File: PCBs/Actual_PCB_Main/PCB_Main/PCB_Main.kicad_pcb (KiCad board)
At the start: 2 copper layers, 145 parts, among them J1 fan connector, J10 To_Speaker_R, J2 10118193-0001LF, J4 10118193-0001LF, J6 XT60-M, J7 HUB75, J9 To_Speaker_L, M1 CSD17581Q3, M2 CSD17581Q3A, Q1 S8050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

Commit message: started PCB Layout
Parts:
- J1: value fan connector -> fanpin
- J2: value 10118193-0001LF -> WBoot
- J4: value 10118193-0001LF -> RBoot
- Q4: value Fan_NMOS -> FanMOS
- R20: footprint Resistor_SMD:R_0815_2038Metric -> Resistor_SMD:R_0805_2012Metric
- U1: value CP2102N-Axx-xQFN28 -> WBootChip
- U9: value CP2102N-Axx-xQFN28 -> RBootChip
- Y2: value CB3LV-3I-40M000000 -> RCLK
- moved J2 178.8 mm to (128.1, 14.3), turned to 180 degrees
- moved C3 162.4 mm to (121.3, 20.6), turned to 90 degrees
- moved Cin1 160.6 mm to (294.4, 172.9)
- moved Cout1 160.6 mm to (280.3, 165.3)
- moved Coutx1 160.6 mm to (293.6, 193.0)
- moved Cres1 160.6 mm to (262.6, 205.7)
- moved Css1 160.6 mm to (277.8, 195.6)
- moved Cvcc1 160.6 mm to (276.9, 202.7)
- moved Dbst1 160.6 mm to (254.0, 205.7)
- moved H1 160.6 mm to (351.5, 285.7)
- moved H2 160.6 mm to (351.5, 278.7)
- moved L1 160.6 mm to (243.8, 172.7)
- moved Rfbt1 160.6 mm to (283.6, 202.4)
- moved Rslope1 160.6 mm to (286.1, 195.6)
- moved Rt1 160.6 mm to (293.0, 182.9)
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- renumbered LightSensorConnector1 to +LightGND, Boot2WROOM1 to WBoot2
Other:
- board text added: "GND"
- board text added: "VDD"

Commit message: PCB reset traces
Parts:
- added Cout1: 560.0 uF, Artisyn_Components:PCAP_SVP_F12_PAN, F.Cu at (257.8, -6.60)
- added Cout1: 560.0 uF, Artisyn_Components:PCAP_SVP_F12_PAN, F.Cu at (257.8, -20.8)
- moved Cvcc1 202.0 mm to (379.4, 28.8)
- moved Rfbt1 202.0 mm to (386.1, 28.4)
- moved Rt1 202.0 mm to (395.6, 8.89)
- moved Coutx1 202.0 mm to (396.1, 19.1)
- moved Cvin1 202.0 mm to (372.7, 29.2)
- moved Cbst1 202.0 mm to (366.7, 22.7)
- moved Rvin1 195.3 mm to (326.5, 11.9)
- moved Cin1 189.9 mm to (223.6, -3.30)
- moved Rfbb1 179.3 mm to (392.2, 46.5)
- moved Rsense1 166.3 mm to (226.3, 33.5), turned to 90 degrees
- moved Cout1 159.0 mm to (257.9, 7.87)
- moved R21 155.9 mm to (89.0, 43.4)
- moved R19 153.5 mm to (89.0, 47.0)
- moved M1 148.3 mm to (252.5, 28.9), turned to -90 degrees
- moved M2 141.4 mm to (263.0, 41.9)
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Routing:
- net TXD0_ROVER: track 0.00 -> 89.0 mm, vias 0 -> 6
- net EN_ROVER: track 0.00 -> 86.0 mm, vias 0 -> 2
- net RXD0_ROVER: track 0.00 -> 65.7 mm, vias 0 -> 4
- net RXD0_WROOM: track 0.00 -> 51.2 mm, vias 0 -> 2
- net TXD0_WROOM: track 0.00 -> 49.1 mm, vias 0 -> 4
- net 3.3V: track 0.00 -> 43.7 mm
- net GND: track 0.00 -> 42.2 mm
- net DTR_WROOM: track 0.00 -> 35.0 mm
- net DTR_ROVER: track 0.00 -> 32.7 mm, vias 0 -> 3
- net RTS_WROOM: track 0.00 -> 27.6 mm, vias 0 -> 3
- net IO0_ROVER: track 0.00 -> 26.3 mm
- net USB_DN_WROOM: track 0.00 -> 20.3 mm, vias 0 -> 2
- net EN_WROOM: track 0.00 -> 19.4 mm
- net USB_DP_ROVER: track 0.00 -> 18.9 mm, vias 0 -> 2
- net VBUS_ROVER: track 0.00 -> 17.5 mm, vias 0 -> 2
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
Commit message: Add files via upload
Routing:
- net 3.3V: track 43.7 -> 64.6 mm
- net GND: track 42.2 -> 61.0 mm
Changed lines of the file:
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@@
   (segment (start 70.104 56.134) (end 72.2395 56.134) (width 0.25) (layer "F.Cu") (net 3))
   (segment (start 67.065 55.38) (end 69.35 55.38) (width 0.25) (layer "F.Cu") (net 3))
+  (segment (start 48.937499 22.712499) (end 53.104999 22.712499) (width 0.25) (layer "F.Cu") (net 4))
   (segment (start 60.96 48.768) (end 60.96 48.26) (width 0.25) (layer "F.Cu") (net 4))
   (segment (start 98.334999 16.839999) (end 95.794999 14.299999) (width 0.25) (layer "F.Cu") (net 4))
+  (segment (start 120.5465 29.464) (end 121.056 29.464) (width 0.25) (layer "F.Cu") (net 4))
   (segment (start 45.72 68.58) (end 47.31 70.17) (width 0.25) (layer "F.Cu") (net 4))
   (segment (start 116.84 20.508) (end 118.11 20.508) (width 0.25) (layer "F.Cu") (net 4))
@@
   (segment (start 105.28 70.358) (end 105.28 69.4925) (width 0.25) (layer "F.Cu") (net 4))
   (segment (start 118.11 20.508) (end 118.684 21.082) (width 0.25) (layer "F.Cu") (net 4))
+  (segment (start 49.408 26.924) (end 49.408 28.954) (width 0.25) (layer "F.Cu") (net 4))
   (segment (start 58.184999 17.639999) (end 59.104999 16.719999) (width 0.25) (layer "F.Cu") (net 4))
+  (segment (start 53.104999 23.227001) (end 49.408 26.924) (width 0.25) (layer "F.Cu") (net 4))
   (segment (start 47.31 70.17) (end 48.26 70.17) (width 0.25) (layer "F.Cu") (net 4))
+  (segment (start 121.056 29.464) (end 125.12 33.528) (width 0.25) (layer "F.Cu") (net 4))
+  (segment (start 53.104999 22.712499) (end 53.104999 23.227001) (width 0.25) (layer "F.Cu") (net 4))
   (segment (start 61.087 49.657) (end 60.96 49.53) (width 0.25) (layer "F.Cu") (net 4))
   (segment (start 62 52.315) (end 62 50.57) (width 0.25) (layer "F.Cu") (net 4))
+  (segment (start 48.024999 21.799999) (end 48.937499 22.712499) (width 0.25) (layer "F.Cu") (net 4))
   (segment (start 62.5 52.315) (end 62.5 50.308) (width 0.25) (layer "F.Cu") (net 4))
   (segment (start 102.74 72.71) (end 102.74 70.996) (width 0.25) (layer "F.Cu") (net 4))
@@
   (segment (start 49.022 60.96) (end 48.768 60.706) (width 0.25) (layer "F.Cu") (net 4))
   (segment (start 58.154999 17.669999) (end 58.184999 17.639999) (width 0.25) (layer "F.Cu") (net 4))
+  (segment (start 49.408 28.954) (end 50.358 29.904) (width 0.25) (layer "F.Cu") (net 4))
   (segment (start 59.104999 16.719999) (end 61.004999 16.719999) (width 0.25) (layer "F.Cu") (net 4))
   (segment (start 113.574999 21.839999) (end 115.508001 21.839999) (width 0.25) (layer "F.Cu") (net 4))
@@
   (segment (start 102.74 74.61) (end 103.69 74.61) (width 0.25) (layer "F.Cu") (net 6))
   (segment (start 241.874 151.226) (end 241.874 150.18) (width 0.25) (layer "F.Cu") (net 6))
+  (segment (start 51.308 26.924) (end 54.488 26.924) (width 0.25) (layer "F.Cu") (net 6))
   (segment (start 64.45 45.654) (end 64.262 45.466) (width 0.25) (layer "F.Cu") (net 6))
   (segment (start 75.33 68.58) (end 72.79 68.58) (width 0.25) (layer "F.Cu") (net 6))
@@
   (segment (start 64.45 48.26) (end 64.45 45.654) (width 0.25) (layer "F.Cu") (net 6))
   (segment (start 242.316 151.668) (end 241.874 151.226) (width 0.25) (layer "F.Cu") (net 6))
+  (segment (start 54.488 23.906998) (end 54.488 26.924) (width 0.25) (layer "F.Cu") (net 6))
+  (segment (start 55.644999 22.749999) (end 54.488 23.906998) (width 0.25) (layer "F.Cu") (net 6))
   (segment (start 45.72 73.66) (end 47.31 72.07) (width 0.25) (layer "F.Cu") (net 6))
   (segment (start 64.516 49.53) (end 64.516 48.768) (width 0.25) (layer "F.Cu") (net 6))
@@
   (segment (start 47.31 72.07) (end 48.26 72.07) (width 0.25) (layer "F.Cu") (net 6))
   (segment (start 58.474999 15.449999) (end 58.184999 15.739999) (width 0.25) (layer "F.Cu") (net 6))
+  (segment (start 132.78 24.209998) (end 134.369999 22.619999) (width 0.25) (layer "F.Cu") (net 6))
   (segment (start 58.154999 15.769999) (end 58.184999 15.739999) (width 0.25) (layer "F.Cu") (net 6))
   (segment (start 63.942 47.752) (end 64.45 48.26) (width 0.25) (layer "F.Cu") (net 6))
@@
   (segment (start 77.43 75.76) (end 77.43 75.732) (width 0.25) (layer "F.Cu") (net 6))
   (segment (start 100.234999 14.939999) (end 100.874999 14.299999) (width 0.25) (layer "F.Cu") (net 6))
+  (segment (start 55.644999 15.769999) (end 48.974999 15.769999) (width 0.25) (layer "F.Cu") (net 6))
   (segment (start 64 50.554) (end 64.008 50.546) (width 0.25) (layer "F.Cu") (net 6))
   (segment (start 100.234999 16.839999) (end 100.234999 14.939999) (width 0.25) (layer "F.Cu") (net 6))
@@
   (segment (start 106.68 73.02) (end 109.22 70.48) (width 0.25) (layer "F.Cu") (net 6))
   (segment (start 55.644999 15.769999) (end 58.154999 15.769999) (width 0.25) (layer "F.Cu") (net 6))
+  (segment (start 132.78 24.892) (end 132.78 24.209998) (width 0.25) (layer "F.Cu") (net 6))
+  (segment (start 48.974999 15.769999) (end 48.024999 16.719999) (width 0.25) (layer "F.Cu") (net 6))
   (segment (start 110.009999 26.904999) (end 110.009999 31.214001) (width 0.25) (layer "F.Cu") (net 8))
   (segment (start 110.009999 31.214001) (end 109.22 32.004) (width 0.25) (layer "F.Cu") (net 8))

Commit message: pcb almost done
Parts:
- added C35: 1000uF, Artisyn_Components:Audio_1000uF, F.Cu at (141.7, 23.4)
- added D2: RED LED, LED_SMD:LED_0805_2012Metric, F.Cu at (136.4, 35.6)
- added R26: 1k, Resistor_SMD:R_0805_2012Metric, F.Cu at (140.2, 36.6)
- J1: value fanpin -> fan connector
- J2: value WBoot -> 10118193-0001LF
- J4: value RBoot -> 10118193-0001LF
- Q4: value FanMOS -> Fan_NMOS
- U1: value WBootChip -> CP2102N-Axx-xQFN28
- U9: value RBootChip -> CP2102N-Axx-xQFN28
- Y2: value RCLK -> CB3LV-3I-40M000000
- moved CsnL1 84.9 mm to (175.2, 105.5)
- moved RsnL1 84.9 mm to (175.2, 110.5)
- moved C0L1 84.0 mm to (189.5, 106.9)
- moved CsnR1 84.0 mm to (162.0, 100.1)
- moved J10 84.0 mm to (136.4, 109.2)
- moved C0R1 84.0 mm to (146.0, 108.7)
- moved CiL1 84.0 mm to (172.2, 100.5)
- moved CiR1 84.0 mm to (157.5, 110.2)
- moved Csc1 84.0 mm to (168.9, 110.3)
- moved J9 84.0 mm to (203.7, 106.4)
- moved RsnR1 84.0 mm to (162.0, 104.8)
- moved U7 84.0 mm to (168.4, 121.4)
- moved C3b1 84.0 mm to (191.2, 120.1)
- moved Cb1 84.0 mm to (161.0, 90.4)
- moved C21 32.6 mm to (137.2, 67.6), turned to 180 degrees
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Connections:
- Boot2ROVER1 pad 2: RXD0_ROVER -> Net-(Boot2ROVER1-RX)
- Boot2ROVER1 pad 3: TXD0_ROVER -> Net-(Boot2ROVER1-TX)
- Rsense1 pad 1: Net-(U5-CSN) -> 5V
- Rsense1 pad 2: 5V -> Net-(U5-CSN)
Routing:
- net WROOM_TO_FANS: track 0.00 -> 135.2 mm, vias 0 -> 4
- net GND: track 61.0 -> 195.1 mm, vias 0 -> 39
- net 5V: track 0.00 -> 99.8 mm
- net AGND: track 0.00 -> 75.2 mm, vias 0 -> 3
- net STB: track 0.00 -> 70.4 mm, vias 0 -> 2
- net C_PIN: track 0.00 -> 67.8 mm, vias 0 -> 3
- net I2S-WS: track 0.00 -> 65.6 mm, vias 0 -> 2
- net A_PIN: track 0.00 -> 61.5 mm, vias 0 -> 2
- net CLK_PIN: track 0.00 -> 59.3 mm, vias 0 -> 2
- net WROOM_TALK_TX: track 0.00 -> 58.6 mm, vias 0 -> 5
- net WROOM_TALK_RX: track 0.00 -> 58.4 mm, vias 0 -> 5
- net B_PIN: track 0.00 -> 58.1 mm, vias 0 -> 1
- net Therm_Reading: track 3.30 -> 60.9 mm
- net I2S_DATA: track 0.00 -> 52.2 mm, vias 0 -> 2
- net EN_WROOM: track 19.4 -> 70.6 mm, vias 0 -> 2
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- added copper zone on F.Cu, net 3.3V
- added copper zone on F.Cu, net 5V
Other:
- board text removed: "VDD"

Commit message: updates to PCB
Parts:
- removed D2: RED LED, LED_SMD:LED_0805_2012Metric
- added D3: RED LED, LED_SMD:LED_0805_2012Metric, F.Cu at (125.4, 38.1)
- added H1: MountingHole, MountingHole:MountingHole_2.7mm, F.Cu at (33.0, 71.1)
- added R22: 0, Resistor_SMD:R_0805_2012Metric, F.Cu at (88.9, 17.8)
- added R23: 0, Resistor_SMD:R_0805_2012Metric, F.Cu at (98.1, 5.08)
- added R24: 0, Resistor_SMD:R_0805_2012Metric, F.Cu at (44.8, 63.5)
- added R25: 0, Resistor_SMD:R_0805_2012Metric, F.Cu at (44.8, 66.0)
- added R27: 1k, Resistor_SMD:R_0805_2012Metric, F.Cu at (131.2, 38.1)
- R26: value 1k -> 0
- moved H2 409.8 mm to (35.6, 17.8)
- moved H3 278.2 mm to (243.8, 15.2)
- moved H1 266.7 mm to (137.2, 127.0)
- moved Coutx1 183.4 mm to (215.9, 53.3), turned to 180 degrees
- moved Rfbb1 174.6 mm to (218.4, 63.5), turned to -90 degrees
- moved H4 173.3 mm to (246.4, 127.0)
- moved Rt1 172.8 mm to (235.3, 73.7)
- moved Rfbt1 170.6 mm to (218.4, 60.0), turned to -90 degrees
- moved Cvcc1 169.3 mm to (218.4, 81.3), turned to 180 degrees
- moved Cbst1 163.4 mm to (218.4, 91.4), turned to 180 degrees
- moved Cvin1 147.5 mm to (234.3, 80.3), turned to 90 degrees
- moved Rvin1 122.0 mm to (231.9, 88.9), turned to 90 degrees
- moved Cout1 78.6 mm to (216.0, 45.7), turned to 180 degrees
- moved Cin1 65.4 mm to (180.3, 45.7)
- moved Cout1 57.2 mm to (215.9, 32.3), turned to 180 degrees
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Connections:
- C3b1 pad 1: Net-(U7-Vcc) -> 14V
- Cout1 pad 1: (no net) -> 14V (x2)
- Cout1 pad 2: (no net) -> GND (x2)
- Cout1 pad 1: Net-(U7-Vcc) -> 14V
- Coutx1 pad 1: Net-(U7-Vcc) -> 14V
- Csc1 pad 1: Net-(U7-Vcc) -> 14V
- M2 pad 5: Net-(U7-Vcc) -> 14V
- M2 pad 6: Net-(U7-Vcc) -> 14V
- M2 pad 7: Net-(U7-Vcc) -> 14V
- M2 pad 8: Net-(U7-Vcc) -> 14V
- M2 pad 9: Net-(U7-Vcc) -> 14V
- R26 pad 1: Net-(D2-K) -> GND
- R26 pad 2: GND -> AGND
- Rfbt1 pad 1: Net-(U7-Vcc) -> 14V
- U7 pad 3: Net-(U7-Vcc) -> 14V
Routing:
- net GND: track 195.1 -> 428.6 mm, vias 39 -> 322
- net 5V: track 99.8 -> 272.3 mm, vias 0 -> 6
- net 3.3V: track 107.2 -> 240.2 mm, vias 0 -> 29
- net Net-(U5-CSN): track 0.00 -> 91.6 mm, vias 0 -> 2
- net 14V: track 0.00 -> 80.5 mm, vias 0 -> 3
- net Net-(M1-D1): track 0.00 -> 56.9 mm, vias 0 -> 4
- net Right_Audio: track 4.75 -> 46.1 mm, vias 1 -> 2
- net Left_Audio: track 7.30 -> 46.6 mm, vias 0 -> 2
- net Net-(U5-FB): track 0.00 -> 38.8 mm, vias 0 -> 2
- net Net-(U7-Vcc): track 33.3 -> 0.00 mm, vias 2 -> 0
- net Net-(U5-UVLO): track 0.00 -> 32.6 mm, vias 0 -> 4
- net Net-(M1-G): track 0.00 -> 28.3 mm, vias 0 -> 2
- net Net-(U5-SS): track 0.00 -> 26.7 mm, vias 0 -> 2
- net RXD0_WROOM: track 51.2 -> 26.2 mm, vias 2 -> 1
- net TXD0_WROOM: track 49.1 -> 26.2 mm, vias 4 -> 3
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- added copper zone on F.Cu, net 14V
- added copper zone on B.Cu, net AGND
- added copper zone on B.Cu, net GND
- added copper zone on F.Cu, net GND

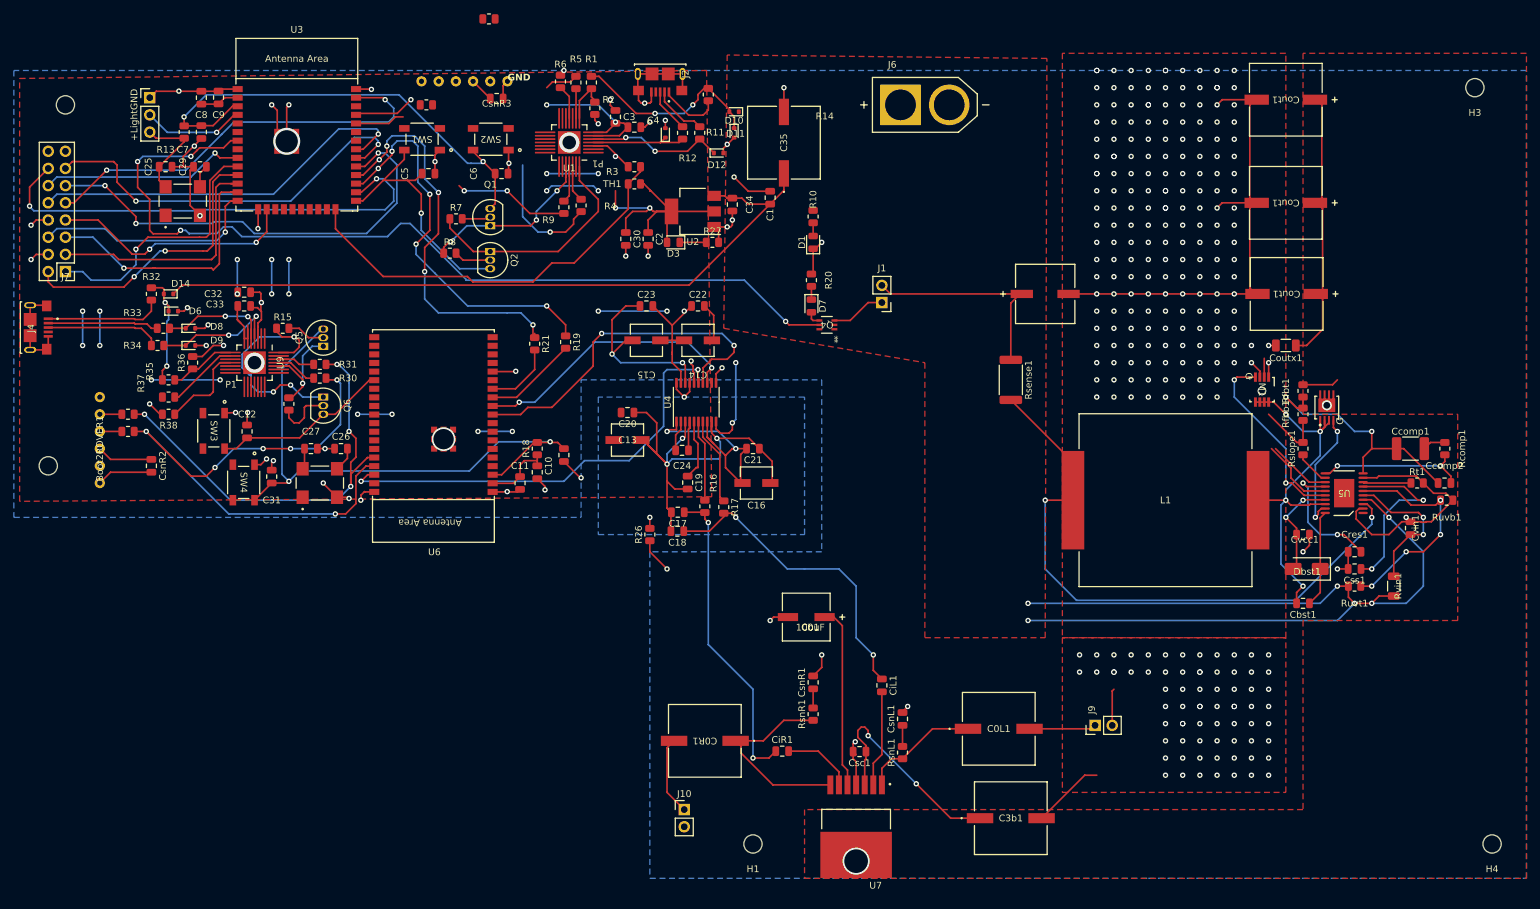
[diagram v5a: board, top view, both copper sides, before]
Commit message: PCB no errors, added PCB sandbox
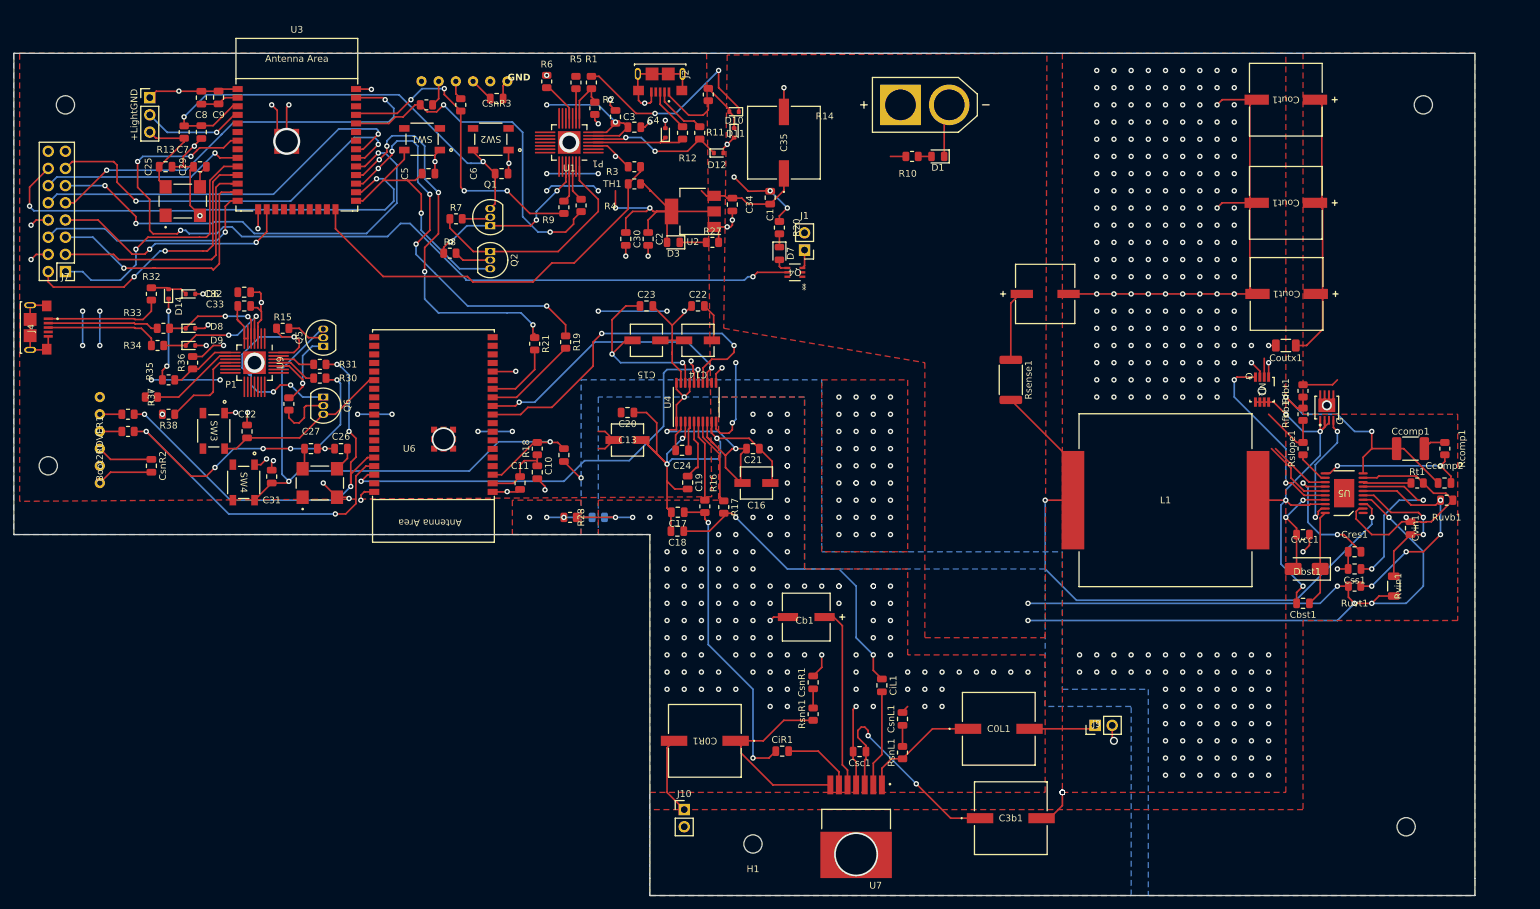
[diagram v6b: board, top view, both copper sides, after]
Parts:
- added R28: 0, Resistor_SMD:R_0805_2012Metric, F.Cu at (110.1, 78.7)
- R26: moved to B.Cu
- moved D1 22.4 mm to (164.5, 25.4), turned to 180 degrees
- moved R10 17.1 mm to (160.7, 25.4), turned to 0 degrees
- moved J1 13.8 mm to (144.8, 39.2)
- moved R23 13.4 mm to (94.0, 17.8), turned to 90 degrees
- moved H4 13.0 mm to (233.7, 124.5)
- moved D7 9.09 mm to (141.1, 39.7)
- moved Q4 9.09 mm to (143.4, 42.5)
- moved R20 9.09 mm to (141.1, 35.9)
- moved R26 8.03 mm to (114.3, 78.7), turned to 0 degrees
- moved H3 8.03 mm to (236.2, 17.8)
- moved D6 3.59 mm to (54.0, 45.7)
- moved R37 2.54 mm to (48.3, 61.0)
- moved R6 2.03 mm to (106.7, 14.3)
- turned D14 to 90 degrees
- turned R22 to 0 degrees
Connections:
- C3b1 pad 2: GND -> AGND
- Cb1 pad 2: GND -> AGND
- Csc1 pad 2: GND -> AGND
- CsnL1 pad 2: GND -> AGND
- CsnR1 pad 2: GND -> AGND
- D10 pad 1: 5V -> VBUS_WROOM
- D10 pad 2: VBUS_WROOM -> Net-(D10-A)
- D11 pad 1: VBUS_WROOM -> Net-(D10-A)
- D14 pad 1: 5V -> VBUS_ROVER
- D14 pad 2: VBUS_ROVER -> Net-(D14-A)
- D6 pad 1: VBUS_ROVER -> Net-(D14-A)
- J10 pad 2: GND -> AGND
- J9 pad 2: GND -> AGND
- R14 pad 2: VBUS_WROOM -> Net-(D10-A)
- R32 pad 2: VBUS_ROVER -> Net-(D14-A)
- U7 pad 4: GND -> AGND
- WBoot2 pad 2: RXD0_WROOM -> Net-(Boot2WROOM1-RX)
- WBoot2 pad 3: TXD0_WROOM -> Net-(Boot2WROOM1-TX)
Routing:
- net 5V: track 272.3 -> 161.9 mm
- net AGND: track 68.6 -> 104.8 mm, vias 4 -> 134
- net RXD0_WROOM: track 26.2 -> 52.0 mm, vias 1 -> 2
- net GND: track 428.6 -> 404.2 mm, vias 322 -> 345
- net TXD0_WROOM: track 26.2 -> 47.1 mm, vias 3 -> 4
- net 3.3V: track 240.2 -> 229.6 mm, vias 29 -> 23
- net Net-(D10-A): track 0.00 -> 7.01 mm
- net WROOM_TO_FANS: track 135.2 -> 128.2 mm
- net Net-(J1-Pin_1): track 8.11 -> 2.78 mm
- net VBUS_ROVER: track 17.5 -> 12.4 mm
- net Net-(D14-A): track 0.00 -> 5.01 mm
- net Net-(Boot2WROOM1-RX): track 0.00 -> 3.85 mm
- net Net-(Boot2WROOM1-TX): track 0.00 -> 2.87 mm
- net Net-(U9-~{RST}): track 10.7 -> 13.3 mm
- net VBUS_WROOM: track 29.0 -> 31.0 mm
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- added copper zone on F.Cu, net AGND
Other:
- board outline added: 215.9 x 124.5 mm
